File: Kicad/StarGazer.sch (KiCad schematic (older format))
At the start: 18 parts, among them U101 STM32G070KBT6

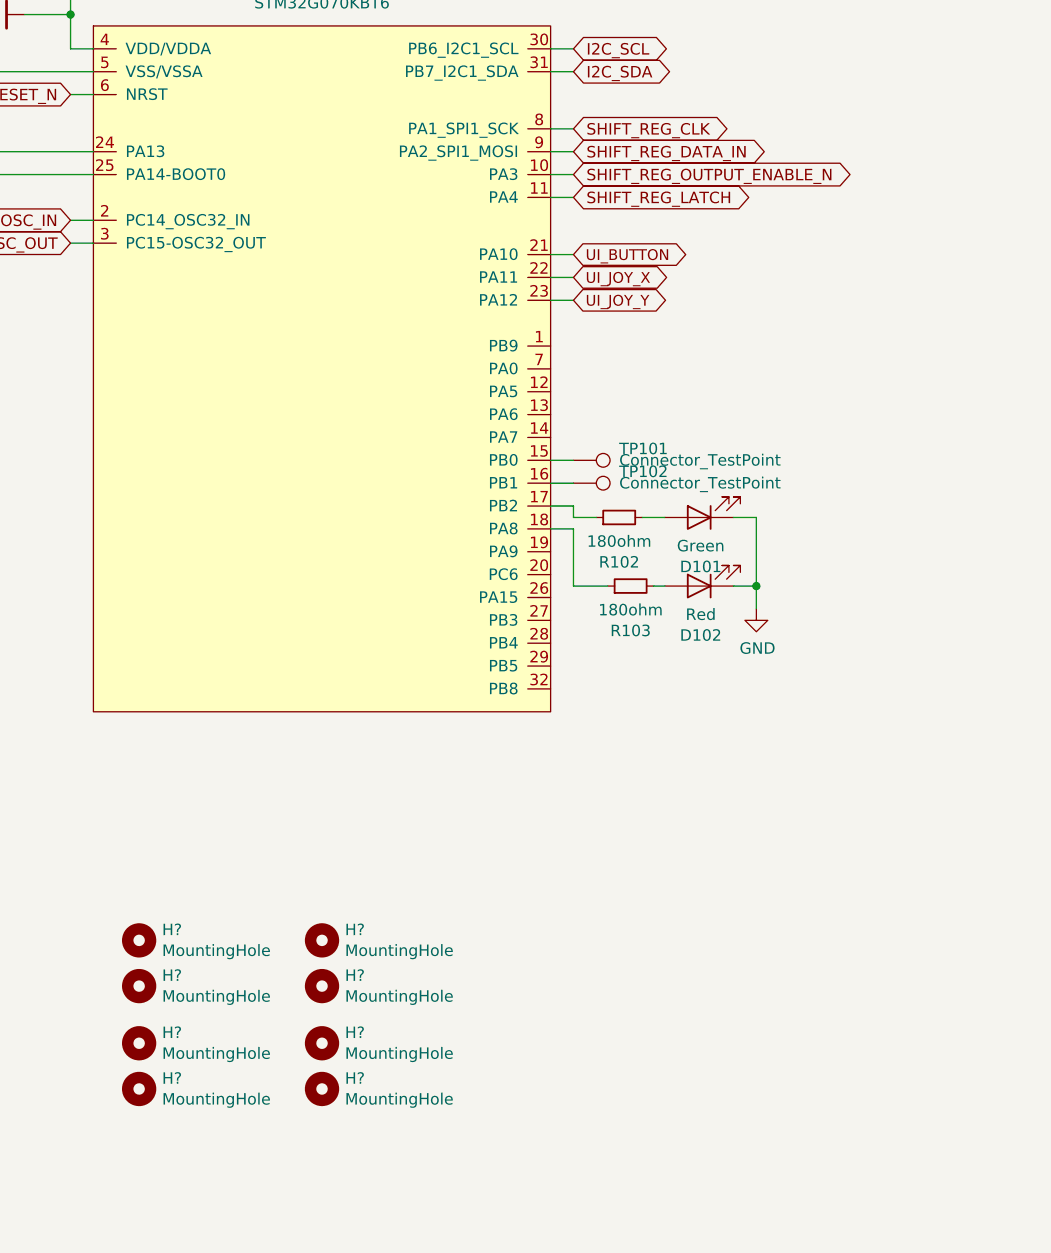
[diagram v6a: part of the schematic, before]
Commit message: PCB updated to curved traces.  Leftover final polish, screw locations, drill-routing, and art is missing
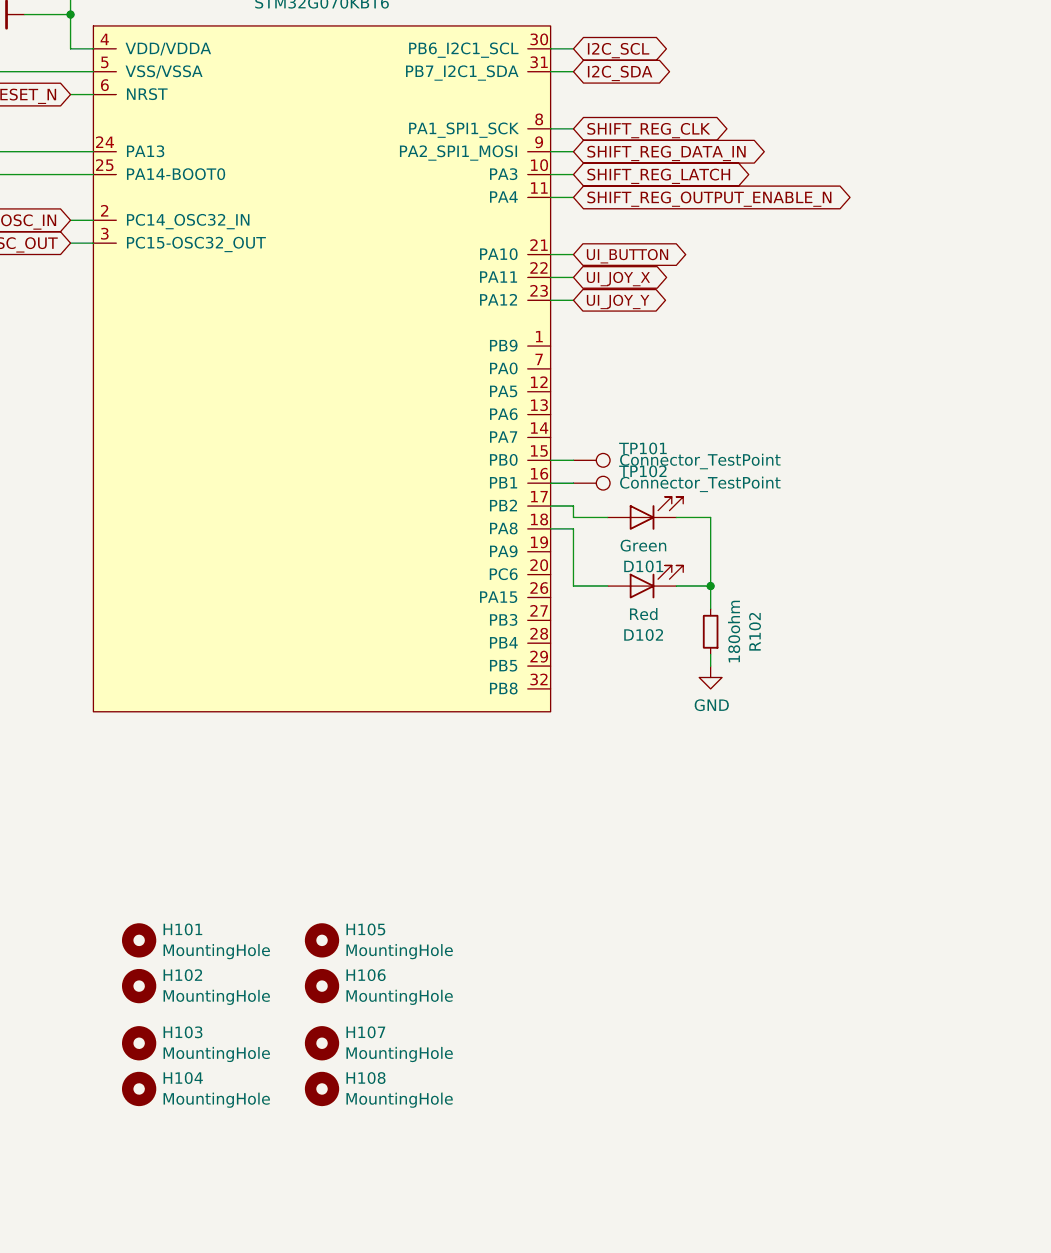
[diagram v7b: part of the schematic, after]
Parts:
- removed R103: 180ohm, Resistor_SMD:R_1206_3216Metric_Pad1.42x1.75mm_HandSolder, symbol Device:R_Small
- gave numbers to parts that had none: 8
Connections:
- net GND: now also R102.1; no longer D101.1 (K), D102.1 (K)
- net SHIFT_REG_LATCH: now also U101.10 (PA3); no longer U101.11 (PA4)
- net SHIFT_REG_OUTPUT_ENABLE_N: now also U101.11 (PA4); no longer U101.10 (PA3)
- net at U101.17 (PB2): now also D101.2 (A); no longer R102.1
- net at U101.18 (PA8): now also D102.2 (A)
- net at R102.2: now also D101.1 (K), D102.1 (K); no longer D101.2 (A)
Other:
- moved on the sheet: D101, D102, R102
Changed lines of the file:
@@
 Text GLabel 6700 2850 2    50   BiDi ~ 0
 I2C_SCL
-Text GLabel 6700 3500 2    50   BiDi ~ 0
+Text GLabel 6700 3400 2    50   BiDi ~ 0
 SHIFT_REG_LATCH
 Text GLabel 6700 3200 2    50   BiDi ~ 0
@@
 F1 "Schematic_Test_Digital.sch" 50
 $EndSheet
-Text GLabel 6700 3400 2    50   BiDi ~ 0
+Text GLabel 6700 3500 2    50   BiDi ~ 0
 SHIFT_REG_OUTPUT_ENABLE_N
 $Comp
@@
 	6600 4750 6700 4750
 $Comp
-L Device:R_Small R103
-U 1 1 5F788165
-P 6950 5200
-AR Path="/5F788165" Ref="R103"  Part="1"
-AR Path="/5F580D08/5F788165" Ref="R?"  Part="1"
-F 0 "R103" V 6754 5200 50  0000 C CNN
-F 1 "180ohm" V 6845 5200 50  0000 C CNN
-F 2 "Resistor_SMD:R_1206_3216Metric_Pad1.42x1.75mm_HandSolder" H 6950 5200 50  0001 C CNN
-F 3 "~" H 6950 5200 50  0001 C CNN
-F 4 "Resistor - LED Status" H 6950 5200 50  0001 C CNN "part_name"
-F 5 "https://www.digikey.com/product-detail/en/stackpole-electronics-inc/RNCP1206FTD180R/RNCP1206FTD180RCT-ND/2240658" H 6950 5200 50  0001 C CNN "part_url"
-	1    6950 5200
-	0    -1   -1   0
-$EndComp
-$Comp
 L Device:R_Small R102
 U 1 1 5F78816D
-P 6900 4900
+P 7300 5400
 AR Path="/5F78816D" Ref="R102"  Part="1"
 AR Path="/5F580D08/5F78816D" Ref="R?"  Part="1"
-F 0 "R102" V 6704 4900 50  0000 C CNN
-F 1 "180ohm" V 6795 4900 50  0000 C CNN
-F 2 "Resistor_SMD:R_1206_3216Metric_Pad1.42x1.75mm_HandSolder" H 6900 4900 50  0001 C CNN
-F 3 "~" H 6900 4900 50  0001 C CNN
-F 4 "Resistor - LED Status" H 6900 4900 50  0001 C CNN "part_name"
-F 5 "https://www.digikey.com/product-detail/en/stackpole-electronics-inc/RNCP1206FTD180R/RNCP1206FTD180RCT-ND/2240658" H 6900 4900 50  0001 C CNN "part_url"
-	1    6900 4900
-	0    -1   -1   0
+F 0 "R102" V 7104 5400 50  0000 C CNN
+F 1 "180ohm" V 7195 5400 50  0000 C CNN
+F 2 "Resistor_SMD:R_1206_3216Metric_Pad1.42x1.75mm_HandSolder" H 7300 5400 50  0001 C CNN
+F 3 "~" H 7300 5400 50  0001 C CNN
+F 4 "Resistor - LED Status" H 7300 5400 50  0001 C CNN "part_name"
+F 5 "https://www.digikey.com/product-detail/en/stackpole-electronics-inc/RNCP1206FTD180R/RNCP1206FTD180RCT-ND/2240658" H 7300 5400 50  0001 C CNN "part_url"
+	1    7300 5400
+	-1   0    0    1
 $EndComp
 $Comp
 L Device:LED D102
 U 1 1 5F788176
-P 7250 5200
+P 7000 5200
 AR Path="/5F788176" Ref="D102"  Part="1"
 AR Path="/5F580D08/5F788176" Ref="D?"  Part="1"
-F 0 "D102" H 7243 5416 50  0000 C CNN
-F 1 "Red" H 7243 5325 50  0000 C CNN
-F 2 "Diode_SMD:D_1206_3216Metric" H 7250 5200 50  0001 C CNN
-F 3 "~" H 7250 5200 50  0001 C CNN
-F 4 "Debug Light" H 7250 5200 50  0001 C CNN "part_details"
-F 5 "https://www.digikey.com/product-detail/en/w%C3%BCrth-elektronik/156120RS75000/732-5030-1-ND/4490054" H 7250 5200 50  0001 C CNN "part_url"
-F 6 "LED - Red" H 7250 5200 50  0001 C CNN "part_name"
-	1    7250 5200
+F 0 "D102" H 6993 5416 50  0000 C CNN
+F 1 "Red" H 6993 5325 50  0000 C CNN
+F 2 "Diode_SMD:D_1206_3216Metric" H 7000 5200 50  0001 C CNN
+F 3 "~" H 7000 5200 50  0001 C CNN
+F 4 "Debug Light" H 7000 5200 50  0001 C CNN "part_details"
+F 5 "https://www.digikey.com/product-detail/en/w%C3%BCrth-elektronik/156120RS75000/732-5030-1-ND/4490054" H 7000 5200 50  0001 C CNN "part_url"
+F 6 "LED - Red" H 7000 5200 50  0001 C CNN "part_name"
+	1    7000 5200
 	-1   0    0    1
 $EndComp
@@
 L Device:LED D101
 U 1 1 5F78817F
-P 7250 4900
+P 7000 4900
 AR Path="/5F78817F" Ref="D101"  Part="1"
 AR Path="/5F580D08/5F78817F" Ref="D?"  Part="1"
-F 0 "D101" H 7243 5116 50  0000 C CNN
-F 1 "Green" H 7243 5025 50  0000 C CNN
-F 2 "Diode_SMD:D_1206_3216Metric" H 7250 4900 50  0001 C CNN
-F 3 "~" H 7250 4900 50  0001 C CNN
-F 4 "Debug Light" H 7250 4900 50  0001 C CNN "part_details"
-F 5 "LED - Green" H 7250 4900 50  0001 C CNN "part_name"
-F 6 "https://www.digikey.com/product-detail/en/w%C3%BCrth-elektronik/156120VS75000/732-5032-1-ND/4490060" H 7250 4900 50  0001 C CNN "part_url"
-	1    7250 4900
+F 0 "D101" H 6993 5116 50  0000 C CNN
+F 1 "Green" H 6993 5025 50  0000 C CNN
+F 2 "Diode_SMD:D_1206_3216Metric" H 7000 4900 50  0001 C CNN
+F 3 "~" H 7000 4900 50  0001 C CNN
+F 4 "Debug Light" H 7000 4900 50  0001 C CNN "part_details"
+F 5 "LED - Green" H 7000 4900 50  0001 C CNN "part_name"
+F 6 "https://www.digikey.com/product-detail/en/w%C3%BCrth-elektronik/156120VS75000/732-5032-1-ND/4490060" H 7000 4900 50  0001 C CNN "part_url"
+	1    7000 4900
 	-1   0    0    1
 $EndComp
 Wire Wire Line
-	7050 5200 7100 5200
-Wire Wire Line
-	7400 5200 7500 5200
-Wire Wire Line
-	7500 5200 7500 4900
-Wire Wire Line
-	7500 4900 7400 4900
-Wire Wire Line
 	6700 4950 6600 4950
 Wire Wire Line
@@
 	6700 4850 6700 4900
 Wire Wire Line
-	6700 4900 6800 4900
-Wire Wire Line
-	7000 4900 7100 4900
-Wire Wire Line
-	7500 5200 7500 5300
-Connection ~ 7500 5200
+	6700 4900 6850 4900
 $Comp
 L power:GND #PWR0103
 U 1 1 5F79138F
-P 7500 5300
-F 0 "#PWR0103" H 7500 5050 50  0001 C CNN
-F 1 "GND" H 7505 5127 50  0000 C CNN
-F 2 "" H 7500 5300 50  0001 C CNN
-F 3 "" H 7500 5300 50  0001 C CNN
-	1    7500 5300
-	1    0    0    -1
-$EndComp
-$Comp
-L Mechanical:MountingHole H?
+P 7300 5550
+F 0 "#PWR0103" H 7300 5300 50  0001 C CNN
+F 1 "GND" H 7305 5377 50  0000 C CNN
+F 2 "" H 7300 5550 50  0001 C CNN
+F 3 "" H 7300 5550 50  0001 C CNN
+	1    7300 5550
+	1    0    0    -1
+$EndComp
+$Comp
+L Mechanical:MountingHole H107
 U 1 1 5F61C377
 P 5600 7200
-F 0 "H?" H 5700 7246 50  0000 L CNN
+F 0 "H107" H 5700 7246 50  0000 L CNN
 F 1 "MountingHole" H 5700 7155 50  0000 L CNN
 F 2 "MountingHole:MountingHole_2.2mm_M2" H 5600 7200 50  0001 C CNN
@@
 $EndComp
 $Comp
-L Mechanical:MountingHole H?
+L Mechanical:MountingHole H108
 U 1 1 5F61C9F3
 P 5600 7400
-F 0 "H?" H 5700 7446 50  0000 L CNN
+F 0 "H108" H 5700 7446 50  0000 L CNN
 F 1 "MountingHole" H 5700 7355 50  0000 L CNN
 F 2 "MountingHole:MountingHole_2.2mm_M2" H 5600 7400 50  0001 C CNN
@@
 $EndComp
 $Comp
-L Mechanical:MountingHole H?
+L Mechanical:MountingHole H105
 U 1 1 5F61EB9F
 P 5600 6750
-F 0 "H?" H 5700 6796 50  0000 L CNN
+F 0 "H105" H 5700 6796 50  0000 L CNN
 F 1 "MountingHole" H 5700 6705 50  0000 L CNN
 F 2 "MountingHole:MountingHole_2.2mm_M2" H 5600 6750 50  0001 C CNN
@@
 $EndComp
 $Comp
-L Mechanical:MountingHole H?
+L Mechanical:MountingHole H106
 U 1 1 5F61EBA6
 P 5600 6950
-F 0 "H?" H 5700 6996 50  0000 L CNN
+F 0 "H106" H 5700 6996 50  0000 L CNN
 F 1 "MountingHole" H 5700 6905 50  0000 L CNN
 F 2 "MountingHole:MountingHole_2.2mm_M2" H 5600 6950 50  0001 C CNN
@@
 $EndComp
 $Comp
-L Mechanical:MountingHole H?
+L Mechanical:MountingHole H103
 U 1 1 5F61FCE3
 P 4800 7200
-F 0 "H?" H 4900 7246 50  0000 L CNN
+F 0 "H103" H 4900 7246 50  0000 L CNN
 F 1 "MountingHole" H 4900 7155 50  0000 L CNN
 F 2 "MountingHole:MountingHole_2.2mm_M2" H 4800 7200 50  0001 C CNN
@@
 $EndComp
 $Comp
-L Mechanical:MountingHole H?
+L Mechanical:MountingHole H104
 U 1 1 5F61FCEA
 P 4800 7400
-F 0 "H?" H 4900 7446 50  0000 L CNN
+F 0 "H104" H 4900 7446 50  0000 L CNN
 F 1 "MountingHole" H 4900 7355 50  0000 L CNN
 F 2 "MountingHole:MountingHole_2.2mm_M2" H 4800 7400 50  0001 C CNN
@@
 $EndComp
 $Comp
-L Mechanical:MountingHole H?
+L Mechanical:MountingHole H101
 U 1 1 5F61FCF1
 P 4800 6750
-F 0 "H?" H 4900 6796 50  0000 L CNN
+F 0 "H101" H 4900 6796 50  0000 L CNN
 F 1 "MountingHole" H 4900 6705 50  0000 L CNN
 F 2 "MountingHole:MountingHole_2.2mm_M2" H 4800 6750 50  0001 C CNN
@@
 $EndComp
 $Comp
-L Mechanical:MountingHole H?
+L Mechanical:MountingHole H102
 U 1 1 5F61FCF8
 P 4800 6950
-F 0 "H?" H 4900 6996 50  0000 L CNN
+F 0 "H102" H 4900 6996 50  0000 L CNN
 F 1 "MountingHole" H 4900 6905 50  0000 L CNN
 F 2 "MountingHole:MountingHole_2.2mm_M2" H 4800 6950 50  0001 C CNN
@@
 	1    0    0    -1
 $EndComp
+Wire Wire Line
+	7150 5200 7300 5200
+Wire Wire Line
+	7300 5200 7300 5300
+Wire Wire Line
+	7150 4900 7300 4900
+Wire Wire Line
+	7300 4900 7300 5200
+Connection ~ 7300 5200
+Wire Wire Line
+	7300 5550 7300 5500
 $EndSCHEMATC
